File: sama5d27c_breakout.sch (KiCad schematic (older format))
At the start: 1 part, among them U1 SAMA5D2x-SIP

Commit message: Connected Unit F
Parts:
- added C?: 10pF, symbol Device:C_Small
- added C? (x4): 12pF, symbol Device:C_Small
- added R? (x5): 100R, symbol Device:R_Small
- added R?: 5.62K, symbol Device:R_Small
- added R?: 10K, symbol Device:R_Small
- added Y?: NX2016SA_24MHz, symbol Device:Crystal_GND24_Small
- added Y?: NX2012SA_32-768KHz, symbol Device:Crystal_Small
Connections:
- net VDDA: now reaches U1.L9 (ADVREF)
- net PIOBU1: now reaches U1.M3 (PIOBU1)
- net PIOBU5: now reaches U1.M5 (PIOBU5)
- net CLK_AUDIO: now reaches U1.N2 (RXD)
- net PIOBU7: now reaches U1.N3 (PIOBU7)
- net PIOBU4: now reaches U1.N4 (PIOBU4)
- net PIOBU6: now reaches U1.N5 (PIOBU6)
- net PIOBU2: now reaches U1.P2 (PIOBU2)
- net LOWQ#: now reaches U1.P3 (PIOBU0)
- net PIOBU3: now reaches U1.P4 (PIOBU3)
- net at U1.R2 (WKUP): now also R?.1
- net at U1.R4 (TST): now also R?.1
- net USBA_M: now reaches U1.T10 (HHSDMA)
- net USBB_M: now reaches U1.T11 (HHSDMB)
- net DATA: now reaches U1.T12 (HHSDPDATC)
- net at U1.T2 (SHDN): now also R?.2
- net at U1.T6 (VBG): now also C?.2, R?.2
- net at U1.T7 (NRST): now also R?.1
- net at U1.T8 (CLK_AUDIO): now also R?.2
- net at U1.U1 (XOUT32): now also C?.1, Y?.2
- net USBA_P: now reaches U1.U10 (HHSDPA)
- net USBB_P: now reaches U1.U11 (HHSDPB)
- net STROBE: now reaches U1.U12 (HHSDMSTRC)
- net at U1.U2 (XIN32): now also C?.1, Y?.1
- net at U1.U6 (COMPP): now also R?.1
- net at U1.U8 (XOUT): now also C?.1, Y?.3
- net at U1.U9 (XIN): now also C?.1, Y?.1
- new net COMPN: R?.1
- new net COMPP: R?.1
- new net GND: C?.2, C?.2, C?.2, C?.2, R?.2, Y?.2, Y?.4
- new net GNDS: C?.1, R?.1
- new net SHDN: R?.2
- new net WKUP: R?.2
- new net nRST: R?.2
- no-connect marks 0 -> 1
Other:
- note added: "24MHz"
- note added: "32KHz"
- moved on the sheet: U1F

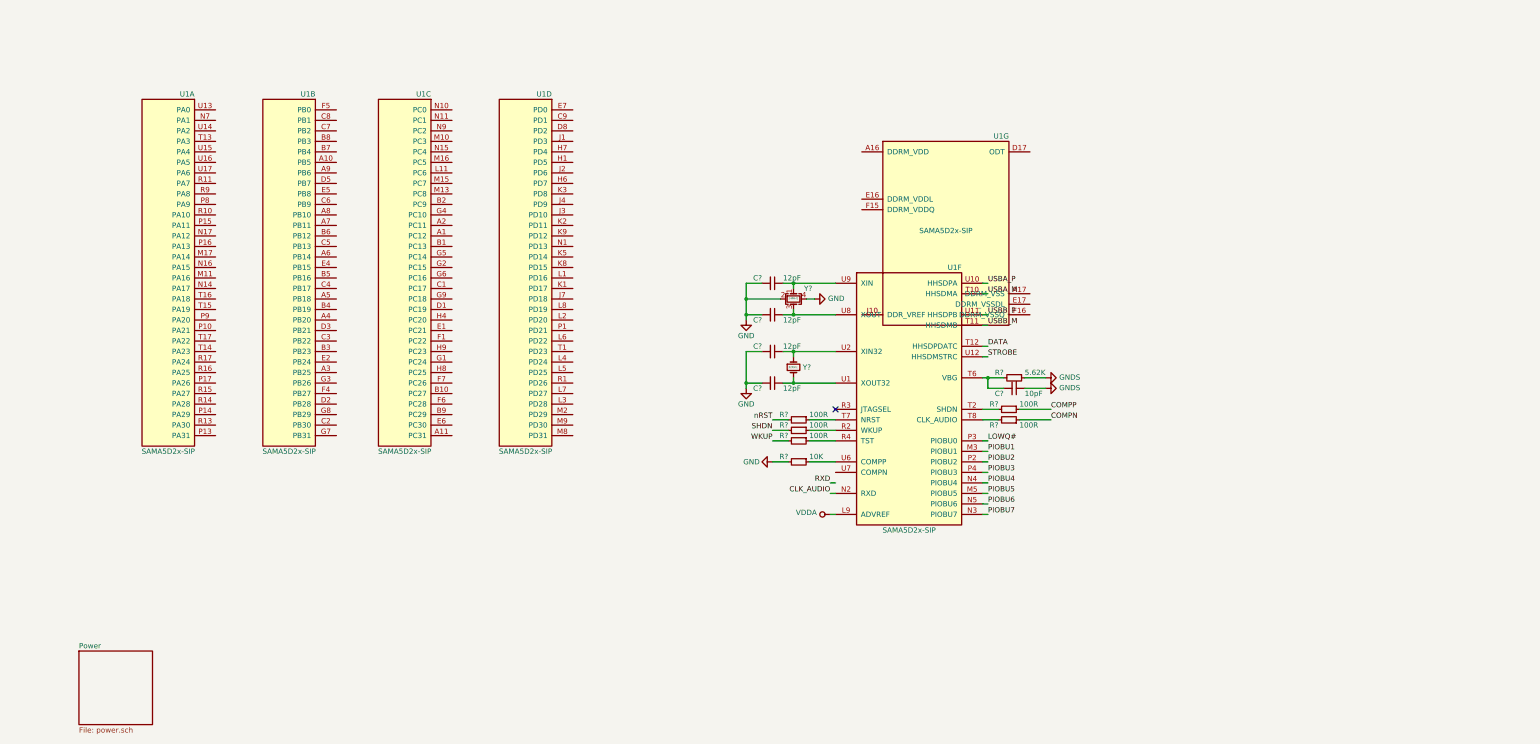
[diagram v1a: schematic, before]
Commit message: Added QSPI Flash and started work on PMIC
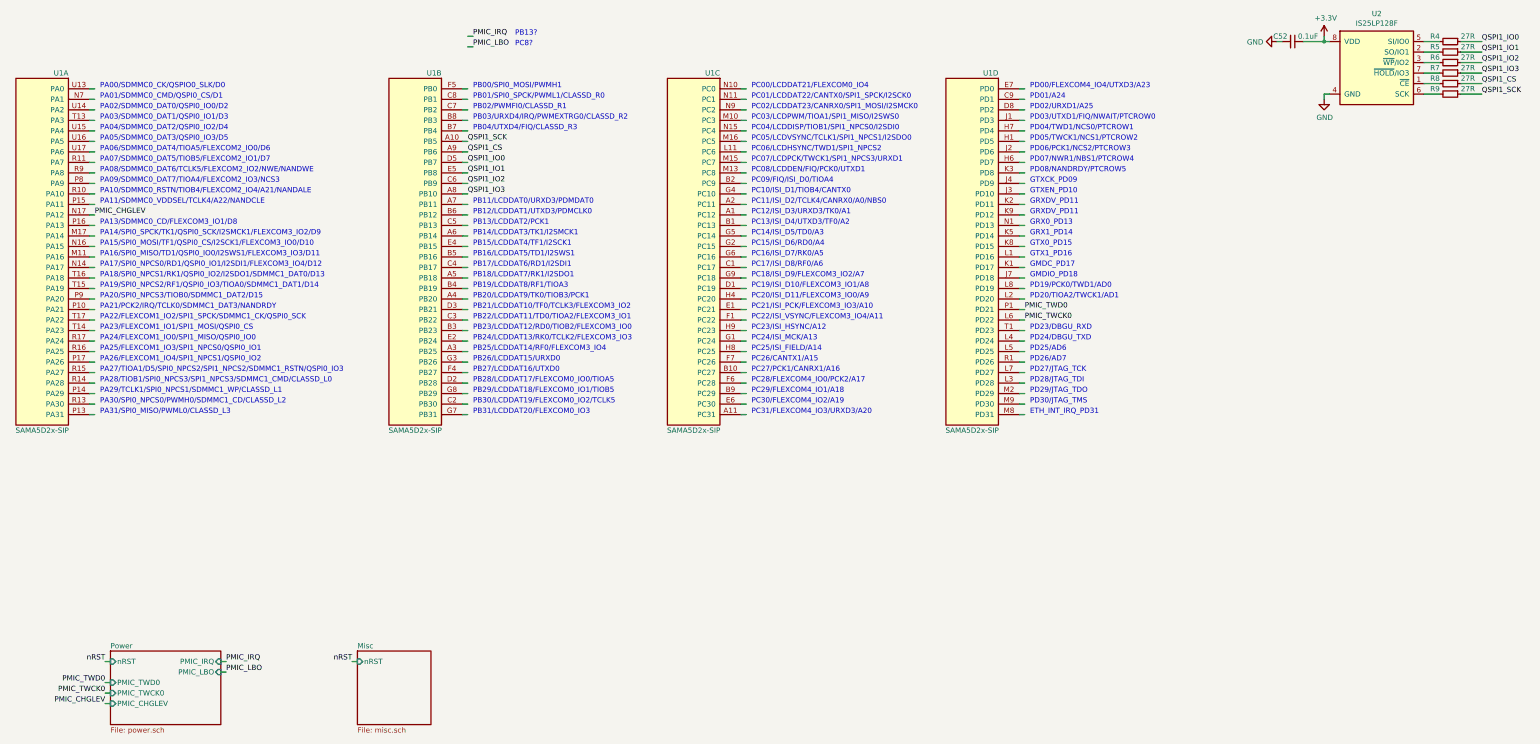
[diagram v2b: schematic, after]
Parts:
- removed C?: 10pF, symbol Device:C_Small
- removed C? (x4): 12pF, symbol Device:C_Small
- removed R? (x5): 100R, symbol Device:R_Small
- removed R?: 5.62K, symbol Device:R_Small
- removed R?: 10K, symbol Device:R_Small
- removed unit 6 of U1
- removed unit 7 of U1
- removed Y?: NX2016SA_24MHz, symbol Device:Crystal_GND24_Small
- removed Y?: NX2012SA_32-768KHz, symbol Device:Crystal_Small
- added C52: 0.1uF, symbol Device:C_Small
- added R4, R5, R6, R7, R8, R9: 27R, symbol Device:R_Small
- added U2: IS25LP128F, Package_SON:WSON-8-1EP_6x5mm_P1.27mm_EP3.4x4mm, symbol Memory_Flash_Extra:IS25LP128F
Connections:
- net labels added: +3.3V, PMIC_CHGLEV, PMIC_IRQ, PMIC_LBO, PMIC_TWCK0, PMIC_TWD0, QSPI1_CS, QSPI1_IO0, QSPI1_IO1, QSPI1_IO2, QSPI1_IO3, QSPI1_SCK
- net labels removed: CLK_AUDIO, COMPN, COMPP, DATA, GNDS, LOWQ#, PIOBU1, PIOBU2, PIOBU3, PIOBU4, PIOBU5, PIOBU6, PIOBU7, RXD, SHDN, STROBE, USBA_M, USBA_P, USBB_M, USBB_P, VDDA, WKUP
- wire segments 58 -> 155
- no-connect marks 1 -> 0
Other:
- note added: "ETH_INT_IRQ_PD31"
- note added: "GMDC_PD17"
- note added: "GMDIO_PD18"
- note added: "GRX0_PD13"
- note added: "GRX1_PD14"
- note added: "GRXDV_PD11"
- note added: "GTX0_PD15"
- note added: "GTX1_PD16"
- note added: "GTXCK_PD09"
- note added: "GTXEN_PD10"
- note added: "PA00/SDMMC0_CK/QSPIO0_SLK/D0\n"
- note added: "PA01/SDMMC0_CMD/QSPI0_CS/D1\n"
- note added: "PA02/SDMMC0_DAT0/QSPI0_IO0/D2\n"
- note added: "PA03/SDMMC0_DAT1/QSPI0_IO1/D3\n"
- note added: "PA04/SDMMC0_DAT2/QSPI0_IO2/D4\n"
- note added: "PA05/SDMMC0_DAT3/QSPI0_IO3/D5\n"
- note added: "PA06/SDMMC0_DAT4/TIOA5/FLEXCOM2_IO0/D6\n"
- note added: "PA07/SDMMC0_DAT5/TIOB5/FLEXCOM2_IO1/D7\n"
- note added: "PA08/SDMMC0_DAT6/TCLK5/FLEXCOM2_IO2/NWE/NANDWE\n"
- note added: "PA09/SDMMC0_DAT7/TIOA4/FLEXCOM2_IO3/NCS3\n"
- note added: "PA10/SDMMC0_RSTN/TIOB4/FLEXCOM2_IO4/A21/NANDALE\n"
- note added: "PA11/SDMMC0_VDDSEL/TCLK4/A22/NANDCLE\n"
- note added: "PA13/SDMMC0_CD/FLEXCOM3_IO1/D8\n"
- note added: "PA14/SPI0_SPCK/TK1/QSPI0_SCK/I2SMCK1/FLEXCOM3_IO2/D9\n"
- note added: "PA15/SPI0_MOSI/TF1/QSPI0_CS/I2SCK1/FLEXCOM3_IO0/D10\n"
- note added: "PA16/SPI0_MISO/TD1/QSPI0_IO0/I2SWS1/FLEXCOM3_IO3/D11\n"
- note added: "PA17/SPI0_NPCS0/RD1/QSPI0_IO1/I2SDI1/FLEXCOM3_IO4/D12\n"
- note added: "PA18/SPI0_NPCS1/RK1/QSPI0_IO2/I2SDO1/SDMMC1_DAT0/D13\n"
- note added: "PA19/SPI0_NPCS2/RF1/QSPI0_IO3/TIOA0/SDMMC1_DAT1/D14\n"
- note added: "PA20/SPI0_NPCS3/TIOB0/SDMMC1_DAT2/D15\n"
- note added: "PA21/PCK2/IRQ/TCLK0/SDMMC1_DAT3/NANDRDY\n"
- note added: "PA22/FLEXCOM1_IO2/SPI1_SPCK/SDMMC1_CK/QSPI0_SCK\n"
- note added: "PA23/FLEXCOM1_IO1/SPI1_MOSI/QSPI0_CS\n"
- note added: "PA24/FLEXCOM1_IO0/SPI1_MISO/QSPI0_IO0\n"
- note added: "PA25/FLEXCOM1_IO3/SPI1_NPCS0/QSPI0_IO1\n"
- note added: "PA26/FLEXCOM1_IO4/SPI1_NPCS1/QSPI0_IO2\n"
- note added: "PA27/TIOA1/D5/SPI0_NPCS2/SPI1_NPCS2/SDMMC1_RSTN/QSPI0_IO3\n"
- note added: "PA28/TIOB1/SPI0_NPCS3/SPI1_NPCS3/SDMMC1_CMD/CLASSD_L0\n"
- note added: "PA29/TCLK1/SPI0_NPCS1/SDMMC1_WP/CLASSD_L1\n"
- note added: "PA30/SPI0_NPCS0/PWMH0/SDMMC1_CD/CLASSD_L2\n"
- note added: "PA31/SPI0_MISO/PWML0/CLASSD_L3\n"
- note added: "PB00/SPI0_MOSI/PWMH1\n"
- note added: "PB01/SPI0_SPCK/PWML1/CLASSD_R0\n"
- note added: "PB02/PWMFI0/CLASSD_R1\n"
- note added: "PB03/URXD4/IRQ/PWMEXTRG0/CLASSD_R2\n"
- note added: "PB04/UTXD4/FIQ/CLASSD_R3\n"
- note added: "PB11/LCDDAT0/URXD3/PDMDAT0\n"
- note added: "PB12/LCDDAT1/UTXD3/PDMCLK0\n"
- note added: "PB13/LCDDAT2/PCK1\n"
- note added: "PB13?"
- note added: "PB14/LCDDAT3/TK1/I2SMCK1\n"
- note added: "PB15/LCDDAT4/TF1/I2SCK1\n"
- note added: "PB16/LCDDAT5/TD1/I2SWS1\n"
- note added: "PB17/LCDDAT6/RD1/I2SDI1\n"
- note added: "PB18/LCDDAT7/RK1/I2SDO1\n"
- note added: "PB19/LCDDAT8/RF1/TIOA3\n"
- note added: "PB20/LCDDAT9/TK0/TIOB3/PCK1\n"
- note added: "PB21/LCDDAT10/TF0/TCLK3/FLEXCOM3_IO2\n"
- note added: "PB22/LCDDAT11/TD0/TIOA2/FLEXCOM3_IO1\n"
- note added: "PB23/LCDDAT12/RD0/TIOB2/FLEXCOM3_IO0\n"
- note added: "PB24/LCDDAT13/RK0/TCLK2/FLEXCOM3_IO3\n"
- note added: "PB25/LCDDAT14/RF0/FLEXCOM3_IO4\n"
- note added: "PB26/LCDDAT15/URXD0\n"
- note added: "PB27/LCDDAT16/UTXD0\n"
- note added: "PB28/LCDDAT17/FLEXCOM0_IO0/TIOA5\n"
- note added: "PB29/LCDDAT18/FLEXCOM0_IO1/TIOB5\n"
- note added: "PB30/LCDDAT19/FLEXCOM0_IO2/TCLK5\n"
- note added: "PB31/LCDDAT20/FLEXCOM0_IO3\n"
- note added: "PC00/LCDDAT21/FLEXCOM0_IO4\n"
- note added: "PC01/LCDDAT22/CANTX0/SPI1_SPCK/I2SCK0\n"
- note added: "PC02/LCDDAT23/CANRX0/SPI1_MOSI/I2SMCK0\n"
- note added: "PC03/LCDPWM/TIOA1/SPI1_MISO/I2SWS0\n"
- note added: "PC04/LCDDISP/TIOB1/SPI1_NPCS0/I2SDI0\n"
- note added: "PC05/LCDVSYNC/TCLK1/SPI1_NPCS1/I2SDO0\n"
- note added: "PC06/LCDHSYNC/TWD1/SPI1_NPCS2\n"
- note added: "PC07/LCDPCK/TWCK1/SPI1_NPCS3/URXD1\n"
- note added: "PC08/LCDDEN/FIQ/PCK0/UTXD1\n"
- note added: "PC09/FIQ/ISI_D0/TIOA4\n"
- note added: "PC10/ISI_D1/TIOB4/CANTX0\n"
- note added: "PC11/ISI_D2/TCLK4/CANRX0/A0/NBS0\n"
- note added: "PC12/ISI_D3/URXD3/TK0/A1\n"
- note added: "PC13/ISI_D4/UTXD3/TF0/A2\n"
- note added: "PC14/ISI_D5/TD0/A3\n"
- note added: "PC15/ISI_D6/RD0/A4\n"
- note added: "PC16/ISI_D7/RK0/A5\n"
- note added: "PC17/ISI_D8/RF0/A6\n"
- note added: "PC18/ISI_D9/FLEXCOM3_IO2/A7\n"
- note added: "PC19/ISI_D10/FLEXCOM3_IO1/A8\n"
- note added: "PC20/ISI_D11/FLEXCOM3_IO0/A9\n"
- note added: "PC21/ISI_PCK/FLEXCOM3_IO3/A10\n"
- note added: "PC22/ISI_VSYNC/FLEXCOM3_IO4/A11\n"
- note added: "PC23/ISI_HSYNC/A12\n"
- note added: "PC24/ISI_MCK/A13\n"
- note added: "PC25/ISI_FIELD/A14\n"
- note added: "PC26/CANTX1/A15\n"
- note added: "PC27/PCK1/CANRX1/A16\n"
- note added: "PC28/FLEXCOM4_IO0/PCK2/A17\n"
- note added: "PC29/FLEXCOM4_IO1/A18\n"
- note added: "PC30/FLEXCOM4_IO2/A19\n"
- note added: "PC31/FLEXCOM4_IO3/URXD3/A20\n"
- note added: "PC8?"
- note added: "PD00/FLEXCOM4_IO4/UTXD3/A23\n"
- note added: "PD01/A24\n"
- note added: "PD02/URXD1/A25\n"
- note added: "PD03/UTXD1/FIQ/NWAIT/PTCROW0\n"
- note added: "PD04/TWD1/NCS0/PTCROW1\n"
- note added: "PD05/TWCK1/NCS1/PTCROW2\n"
- note added: "PD06/PCK1/NCS2/PTCROW3\n"
- note added: "PD07/NWR1/NBS1/PTCROW4\n"
- note added: "PD08/NANDRDY/PTCROW5\n"
- note added: "PD19/PCK0/TWD1/AD0\n"
- note added: "PD20/TIOA2/TWCK1/AD1\n"
- note added: "PD23/DBGU_RXD\n"
- note added: "PD24/DBGU_TXD\n"
- note added: "PD25/AD6\n"
- note added: "PD26/AD7\n"
- note added: "PD27/JTAG_TCK\n"
- note added: "PD28/JTAG_TDI\n"
- note added: "PD29/JTAG_TDO\n"
- note added: "PD30/JTAG_TMS\n"
- note removed: "24MHz"
- note removed: "32KHz"
- moved on the sheet: U1A, U1B, U1C, U1D

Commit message: Finished power, added microSD, USB A, btn
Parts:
- added C?: 20pF, symbol Device:C_Small
- added C?: 0.1uF, symbol Device:C_Small
- added FB?: BLM03AX100SZ1, Inductor_SMD:L_0603_1608Metric, symbol Device:Ferrite_Bead_Small
- added J?: Micro_SD_Card_Det, symbol Connector:Micro_SD_Card_Det
- added J?: USB_B_Micro, symbol Connector:USB_B_Micro
- added R? (x2): 10K, symbol Device:R_Small
- added R?: 0R, symbol Device:R_Small
- added R?: 100R, symbol Device:R_Small
- added R?: 100K, symbol Device:R_Small
- added R?: 200K, symbol Device:R_Small
- added RN?: 68K, Resistor_THT:R_Array_SIP5, symbol Device:R_Network04
- added SW?: SW_USR, symbol Switch:SW_SPST
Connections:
- net labels added: JTAG_TCK, JTAG_TDI, JTAG_TDO, JTAG_TMS, SDMMC0_CK, SDMMC0_CMD, SDMMC0_DAT0, SDMMC0_DAT1, SDMMC0_DAT2, SDMMC1_CD, SDMMC1_CDA, SDMMC1_CK, SDMMC1_DAT0, SDMMC1_DAT1, SDMMC1_DAT2, SDMMC1_DAT3, SHDN, USBA_D+, USBA_D-, USBA_VBUS_5V, USBB_D+, USBB_D-, USR_BTN, VBUS, WKUP
- wire segments 155 -> 220
- no-connect marks 0 -> 1
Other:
- note added: "TODO: RGB LED"
- note added: "USB traces\nMax mismatch 3.8mm\n90 ohm impedance"
- note removed: "PA00/SDMMC0_CK/QSPIO0_SLK/D0\n"
- note removed: "PA01/SDMMC0_CMD/QSPI0_CS/D1\n"
- note removed: "PA02/SDMMC0_DAT0/QSPI0_IO0/D2\n"
- note removed: "PA03/SDMMC0_DAT1/QSPI0_IO1/D3\n"
- note removed: "PA04/SDMMC0_DAT2/QSPI0_IO2/D4\n"
- note removed: "PA18/SPI0_NPCS1/RK1/QSPI0_IO2/I2SDO1/SDMMC1_DAT0/D13\n"
- note removed: "PA19/SPI0_NPCS2/RF1/QSPI0_IO3/TIOA0/SDMMC1_DAT1/D14\n"
- note removed: "PA20/SPI0_NPCS3/TIOB0/SDMMC1_DAT2/D15\n"
- note removed: "PA21/PCK2/IRQ/TCLK0/SDMMC1_DAT3/NANDRDY\n"
- note removed: "PA22/FLEXCOM1_IO2/SPI1_SPCK/SDMMC1_CK/QSPI0_SCK\n"
- note removed: "PA28/TIOB1/SPI0_NPCS3/SPI1_NPCS3/SDMMC1_CMD/CLASSD_L0\n"
- note removed: "PA29/TCLK1/SPI0_NPCS1/SDMMC1_WP/CLASSD_L1\n"
- note removed: "PA30/SPI0_NPCS0/PWMH0/SDMMC1_CD/CLASSD_L2\n"
- note removed: "PD20/TIOA2/TWCK1/AD1\n"
- note removed: "PD27/JTAG_TCK\n"
- note removed: "PD28/JTAG_TDI\n"
- note removed: "PD29/JTAG_TDO\n"
- note removed: "PD30/JTAG_TMS\n"

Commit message: Finish schematic (?), set footprints and start placement
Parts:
- removed C52, C?: 0.1uF, symbol Device:C_Small
- removed C?: 20pF, symbol Device:C_Small
- removed FB?: BLM03AX100SZ1, Inductor_SMD:L_0603_1608Metric, symbol Device:Ferrite_Bead_Small
- removed J?: Micro_SD_Card_Det, symbol Connector:Micro_SD_Card_Det
- removed J?: USB_B_Micro, symbol Connector:USB_B_Micro
- removed R4, R5, R6, R7, R8, R9: 27R, symbol Device:R_Small
- removed R? (x2): 10K, symbol Device:R_Small
- removed R?: 0R, symbol Device:R_Small
- removed R?: 100R, symbol Device:R_Small
- removed R?: 100K, symbol Device:R_Small
- removed R?: 200K, symbol Device:R_Small
- removed RN?: 68K, Resistor_THT:R_Array_SIP5, symbol Device:R_Network04
- removed SW?: SW_USR, symbol Switch:SW_SPST
- removed U2: IS25LP128F, Package_SON:WSON-8-1EP_6x5mm_P1.27mm_EP3.4x4mm, symbol Memory_Flash_Extra:IS25LP128F
- added J1: Conn_LCD, Connector_PinHeader_1.27mm:PinHeader_2x21_P1.27mm_Vertical, symbol Connector_Generic:Conn_02x21_Odd_Even
- added J2: Conn_JTAG, Connector_PinHeader_2.54mm:PinHeader_1x07_P2.54mm_Vertical, symbol Connector_Generic:Conn_01x07
- added J3: Conn_SDMMC0, Connector_PinHeader_2.54mm:PinHeader_2x07_P2.54mm_Vertical, symbol Connector_Generic:Conn_02x07_Odd_Even
- added J4: Conn_FLEXCOM3_4, Connector_PinHeader_2.54mm:PinHeader_2x06_P2.54mm_Vertical, symbol Connector_Generic:Conn_02x06_Odd_Even
- added J5: Conn_DBGU, Connector_PinHeader_2.54mm:PinHeader_1x03_P2.54mm_Vertical, symbol Connector_Generic:Conn_01x03
- added R1, R2: 4.7K, Resistor_SMD:R_0603_1608Metric, symbol Device:R_Small
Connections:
- net labels added: CLASSD_R0, CLASSD_R1, CLASSD_R2, CLASSD_R3, DBGU_RX, DBGU_TX, FLEXCOM3_IO0, FLEXCOM3_IO1, FLEXCOM3_IO2, FLEXCOM3_IO3, FLEXCOM3_IO4, FLEXCOM4_IO0, FLEXCOM4_IO1, FLEXCOM4_IO2, FLEXCOM4_IO3, FLEXCOM4_IO4, IRQ1, IRQ2, LCD_DAT0, LCD_DAT1, LCD_DAT10, LCD_DAT11, LCD_DAT12, LCD_DAT13, LCD_DAT14, LCD_DAT15, LCD_DAT16, LCD_DAT17, LCD_DAT18, LCD_DAT19, LCD_DAT2, LCD_DAT20, LCD_DAT21, LCD_DAT22, LCD_DAT23, LCD_DAT3, LCD_DAT4, LCD_DAT5, LCD_DAT6, LCD_DAT7, LCD_DAT8, LCD_DAT9, LCD_DEN, LCD_DISP, LCD_HSYNC, LCD_PCK, LCD_PWM, LCD_TWCK, LCD_TWD, LCD_VSYNC, LED_BLUE, LED_GREEN, LED_RED, PMIC_TWCK, PMIC_TWD, SDMMC0_CD, SDMMC0_CDA, SDMMC0_DAT3, SDMMC0_DAT4, SDMMC0_DAT5, SDMMC0_DAT6, SDMMC0_DAT7, SDMMC0_VDDSEL, SPI0_MISO, SPI0_MOSI, SPI0_NPCS0, SPI0_SPCK, USBB_OVERCURR, USBB_PWR_EN
- net labels removed: PMIC_TWCK0, PMIC_TWD0, SDMMC0_CMD, USBA_D+, USBA_D-, USBB_D+, USBB_D-, VBUS
- wire segments 220 -> 250
- no-connect marks 1 -> 34
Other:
- note removed: "PA05/SDMMC0_DAT3/QSPI0_IO3/D5\n"
- note removed: "PA06/SDMMC0_DAT4/TIOA5/FLEXCOM2_IO0/D6\n"
- note removed: "PA07/SDMMC0_DAT5/TIOB5/FLEXCOM2_IO1/D7\n"
- note removed: "PA08/SDMMC0_DAT6/TCLK5/FLEXCOM2_IO2/NWE/NANDWE\n"
- note removed: "PA09/SDMMC0_DAT7/TIOA4/FLEXCOM2_IO3/NCS3\n"
- note removed: "PA10/SDMMC0_RSTN/TIOB4/FLEXCOM2_IO4/A21/NANDALE\n"
- note removed: "PA11/SDMMC0_VDDSEL/TCLK4/A22/NANDCLE\n"
- note removed: "PA13/SDMMC0_CD/FLEXCOM3_IO1/D8\n"
- note removed: "PA14/SPI0_SPCK/TK1/QSPI0_SCK/I2SMCK1/FLEXCOM3_IO2/D9\n"
- note removed: "PA15/SPI0_MOSI/TF1/QSPI0_CS/I2SCK1/FLEXCOM3_IO0/D10\n"
- note removed: "PA16/SPI0_MISO/TD1/QSPI0_IO0/I2SWS1/FLEXCOM3_IO3/D11\n"
- note removed: "PA17/SPI0_NPCS0/RD1/QSPI0_IO1/I2SDI1/FLEXCOM3_IO4/D12\n"
- note removed: "PA27/TIOA1/D5/SPI0_NPCS2/SPI1_NPCS2/SDMMC1_RSTN/QSPI0_IO3\n"
- note removed: "PA31/SPI0_MISO/PWML0/CLASSD_L3\n"
- note removed: "PB00/SPI0_MOSI/PWMH1\n"
- note removed: "PB01/SPI0_SPCK/PWML1/CLASSD_R0\n"
- note removed: "PB02/PWMFI0/CLASSD_R1\n"
- note removed: "PB03/URXD4/IRQ/PWMEXTRG0/CLASSD_R2\n"
- note removed: "PB04/UTXD4/FIQ/CLASSD_R3\n"
- note removed: "PB11/LCDDAT0/URXD3/PDMDAT0\n"
- note removed: "PB12/LCDDAT1/UTXD3/PDMCLK0\n"
- note removed: "PB13/LCDDAT2/PCK1\n"
- note removed: "PB13?"
- note removed: "PB14/LCDDAT3/TK1/I2SMCK1\n"
- note removed: "PB15/LCDDAT4/TF1/I2SCK1\n"
- note removed: "PB16/LCDDAT5/TD1/I2SWS1\n"
- note removed: "PB17/LCDDAT6/RD1/I2SDI1\n"
- note removed: "PB18/LCDDAT7/RK1/I2SDO1\n"
- note removed: "PB19/LCDDAT8/RF1/TIOA3\n"
- note removed: "PB20/LCDDAT9/TK0/TIOB3/PCK1\n"
- note removed: "PB21/LCDDAT10/TF0/TCLK3/FLEXCOM3_IO2\n"
- note removed: "PB22/LCDDAT11/TD0/TIOA2/FLEXCOM3_IO1\n"
- note removed: "PB23/LCDDAT12/RD0/TIOB2/FLEXCOM3_IO0\n"
- note removed: "PB24/LCDDAT13/RK0/TCLK2/FLEXCOM3_IO3\n"
- note removed: "PB25/LCDDAT14/RF0/FLEXCOM3_IO4\n"
- note removed: "PB26/LCDDAT15/URXD0\n"
- note removed: "PB27/LCDDAT16/UTXD0\n"
- note removed: "PB28/LCDDAT17/FLEXCOM0_IO0/TIOA5\n"
- note removed: "PB29/LCDDAT18/FLEXCOM0_IO1/TIOB5\n"
- note removed: "PB30/LCDDAT19/FLEXCOM0_IO2/TCLK5\n"
- note removed: "PB31/LCDDAT20/FLEXCOM0_IO3\n"
- note removed: "PC00/LCDDAT21/FLEXCOM0_IO4\n"
- note removed: "PC01/LCDDAT22/CANTX0/SPI1_SPCK/I2SCK0\n"
- note removed: "PC02/LCDDAT23/CANRX0/SPI1_MOSI/I2SMCK0\n"
- note removed: "PC03/LCDPWM/TIOA1/SPI1_MISO/I2SWS0\n"
- note removed: "PC04/LCDDISP/TIOB1/SPI1_NPCS0/I2SDI0\n"
- note removed: "PC05/LCDVSYNC/TCLK1/SPI1_NPCS1/I2SDO0\n"
- note removed: "PC06/LCDHSYNC/TWD1/SPI1_NPCS2\n"
- note removed: "PC07/LCDPCK/TWCK1/SPI1_NPCS3/URXD1\n"
- note removed: "PC08/LCDDEN/FIQ/PCK0/UTXD1\n"
- note removed: "PC09/FIQ/ISI_D0/TIOA4\n"
- note removed: "PC10/ISI_D1/TIOB4/CANTX0\n"
- note removed: "PC18/ISI_D9/FLEXCOM3_IO2/A7\n"
- note removed: "PC19/ISI_D10/FLEXCOM3_IO1/A8\n"
- note removed: "PC20/ISI_D11/FLEXCOM3_IO0/A9\n"
- note removed: "PC21/ISI_PCK/FLEXCOM3_IO3/A10\n"
- note removed: "PC22/ISI_VSYNC/FLEXCOM3_IO4/A11\n"
- note removed: "PC25/ISI_FIELD/A14\n"
- note removed: "PC28/FLEXCOM4_IO0/PCK2/A17\n"
- note removed: "PC29/FLEXCOM4_IO1/A18\n"
- note removed: "PC30/FLEXCOM4_IO2/A19\n"
- note removed: "PC31/FLEXCOM4_IO3/URXD3/A20\n"
- note removed: "PC8?"
- note removed: "PD00/FLEXCOM4_IO4/UTXD3/A23\n"
- note removed: "PD01/A24\n"
- note removed: "PD02/URXD1/A25\n"
- note removed: "PD03/UTXD1/FIQ/NWAIT/PTCROW0\n"
- note removed: "PD04/TWD1/NCS0/PTCROW1\n"
- note removed: "PD05/TWCK1/NCS1/PTCROW2\n"
- note removed: "PD19/PCK0/TWD1/AD0\n"
- note removed: "TODO: RGB LED"
- note removed: "USB traces\nMax mismatch 3.8mm\n90 ohm impedance"
- moved on the sheet: U1A, U1B, U1C, U1D
